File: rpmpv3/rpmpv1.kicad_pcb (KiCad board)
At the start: 2 copper layers, 85.7 x 64.4 mm, 16 parts, among them J1 RPi_GPIO, J2 RPi_GPIO, J3 TEST_1P, J4 TEST_1P, J5 TEST_1P, P1 CONN_02X25, U1 74LS245, U2 74LS245, U3 74LS245, U4 74LS245, U5 74LS05

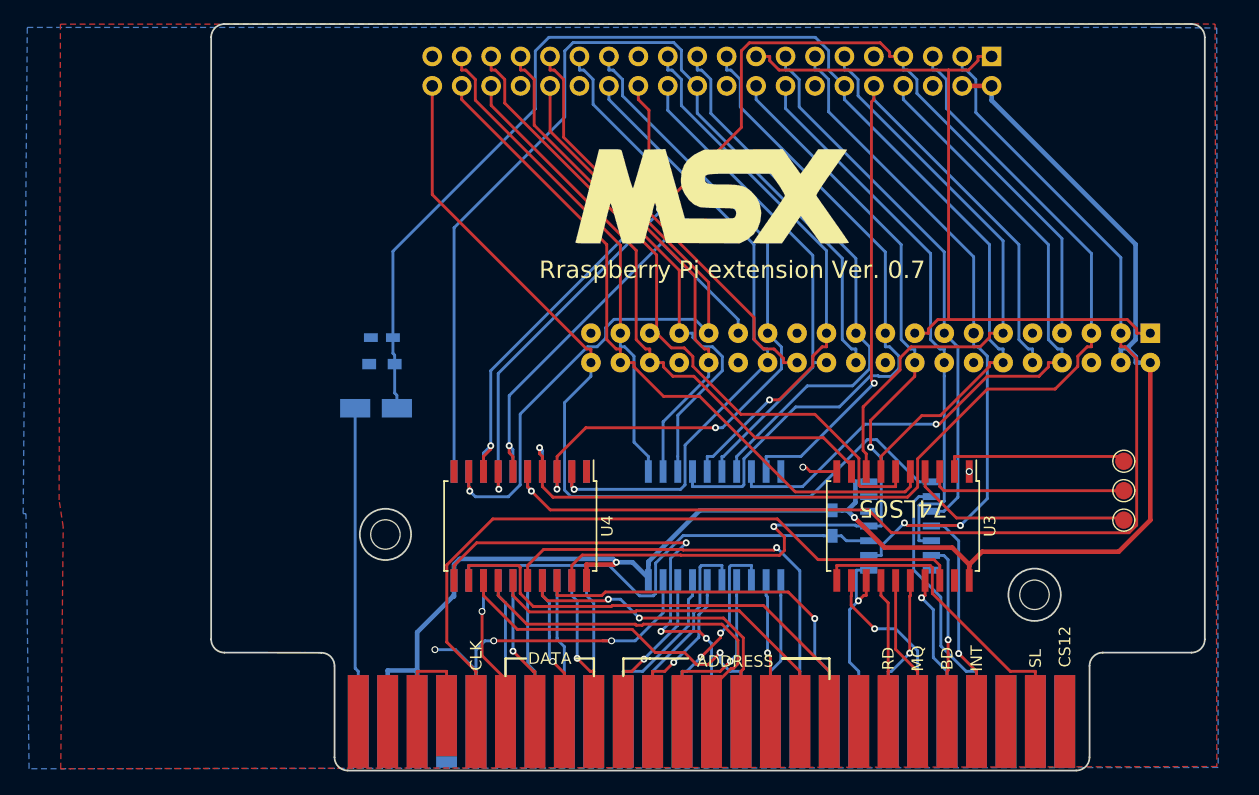
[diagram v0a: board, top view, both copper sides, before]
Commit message: update for RPMP V3
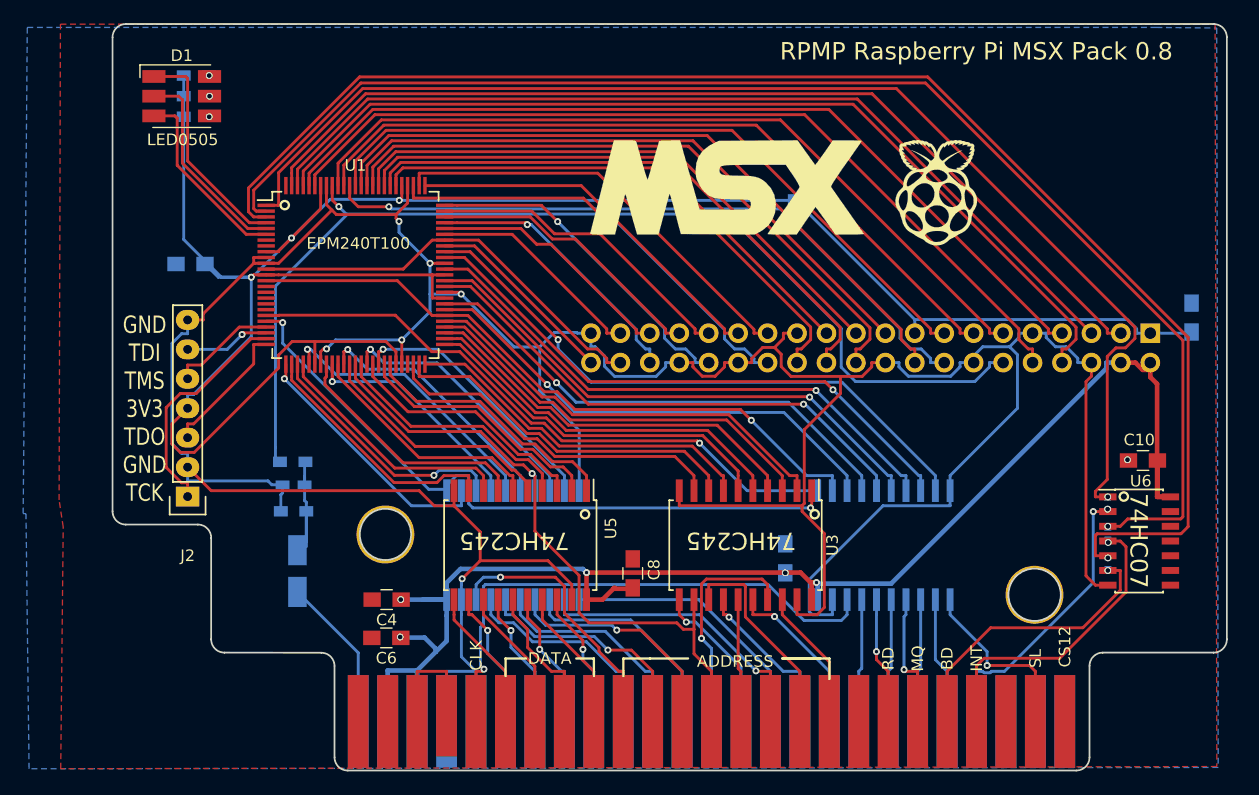
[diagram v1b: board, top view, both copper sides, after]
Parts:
- removed J3, J4, J5: TEST_1P, TestPoint:TestPoint_Pad_D1.5mm
- added C10: C, Capacitors_SMD:C_0805_HandSoldering, F.Cu at (194.7, 87.3)
- added C3: C, Capacitors_SMD:C_0805_HandSoldering, B.Cu at (112.5, 70.4)
- added C4: C, Capacitors_SMD:C_0805_HandSoldering, F.Cu at (129.4, 99.3)
- added C5: C, Capacitors_SMD:C_0805_HandSoldering, B.Cu at (166.1, 65.0)
- added C6: C, Capacitors_SMD:C_0805_HandSoldering, F.Cu at (129.4, 102.6)
- added C7: C, Capacitors_SMD:C_0805_HandSoldering, B.Cu at (198.9, 75.0)
- added C8: C, Capacitors_SMD:C_0805_HandSoldering, F.Cu at (150.7, 97.1)
- added C9: C, Capacitors_SMD:C_0805_HandSoldering, B.Cu at (163.8, 95.8)
- added D1: LED_RGB, LEDs:LED_RGB_5050-6, F.Cu at (111.8, 55.9)
- added G***: LOGO, MSX:raspberry_pi_logo, F.Cu at (176.9, 64.2)
- added G2: LOGO, MSX:msx-logo, B.Cu at (185.3, 57.2)
- added R3: R, Resistors_SMD:R_0603_HandSoldering, B.Cu at (113.0, 57.7)
- added R4: R, Resistors_SMD:R_0603_HandSoldering, B.Cu at (121.4, 91.7)
- added R5: R, Resistors_SMD:R_0402_NoSilk, B.Cu at (191.7, 96.2)
- added R6: R, Resistors_SMD:R_0402_NoSilk, B.Cu at (191.6, 91.1)
- added R7: R, Resistors_SMD:R_0402_NoSilk, B.Cu at (191.7, 93.6)
- added R8: R, Resistors_SMD:R_0603_HandSoldering, B.Cu at (121.3, 87.4)
- added U6: 74LS05, Housings_SOIC:SOIC-14_3.9x8.7mm_Pitch1.27mm, F.Cu at (194.4, 94.3)
- J2: value RPi_GPIO -> Conn_01x07; footprint Socket_Strips:Socket_Strip_Straight_2x20_Pitch2.54mm -> Pin_Headers:Pin_Header_Straight_1x07; moved to F.Cu
- U1: value 74LS245 -> MaxII_EPM240; footprint Housings_SOIC:SOIC-20W_7.5x12.8mm_Pitch1.27mm -> Housings_QFP:TQFP-100_14x14mm_Pitch0.5mm; moved to F.Cu
- U4: moved to B.Cu
- U5: value 74LS05 -> 74LS245; footprint Housings_SOIC:SOIC-14_3.9x8.7mm_Pitch1.27mm -> Housings_SOIC:SOIC-20W_7.5x12.8mm_Pitch1.27mm; moved to F.Cu
- moved J2 79.1 mm to (112.3, 90.4), turned to 180 degrees
- moved R1 67.1 mm to (113.0, 54.1), turned to 0 degrees
- moved U1 37.8 mm to (126.7, 71.3), turned to 0 degrees
- moved U5 32.8 mm to (141.0, 94.6), turned to 270 degrees
- moved U2 31.4 mm to (172.3, 94.6)
- moved R2 28.1 mm to (113.0, 55.9), turned to 0 degrees
- moved C2 15.6 mm to (121.7, 96.9), turned to 270 degrees
- moved C1 14.8 mm to (121.4, 89.4)
- moved U3 13.7 mm to (160.4, 94.6)
- moved U4 1.77 mm to (140.3, 94.6)
- moved G*** 1.48 mm to (158.8, 63.8)
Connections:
- C1 pad 1: /RC18 -> Net-(C1-Pad1)
- C2 pad 1: /RC18 -> Net-(C1-Pad1)
- J2 pad 1: +3V3 -> /TCK
- J2 pad 2: +5V -> GND
- J2 pad 3: /RD2 -> /TDO
- J2 pad 4: +5V -> +3V3
- J2 pad 5: /RD3 -> /TMS
- J2 pad 6: GND -> /TDI
- J2 pad 7: /RD4 -> GND
- R1 pad 1: /nRC24 -> +3V3
- R1 pad 2: +5V -> Net-(D1-Pad6)
- R2 pad 1: /RC18 -> +3V3
- R2 pad 2: GND -> Net-(D1-Pad5)
- U1 pad 1: /RC26 -> /WAIT3
- U1 pad 11: /A7 -> GND
- U1 pad 12: /A6 -> /RC20
- U1 pad 13: /A1 -> +3V3
- U1 pad 14: /A0 -> /CLK3
- U1 pad 15: /A3 -> Net-(U1-Pad15)
- U1 pad 16: /A2 -> Net-(U1-Pad16)
- U1 pad 17: /A5 -> Net-(U1-Pad17)
- U1 pad 18: /A4 -> Net-(U1-Pad18)
- U1 pad 19: GND -> Net-(U1-Pad19)
- U1 pad 2: /RA12 -> /INT3
- U1 pad 20: +5V -> /CD
- U1 pad 3: /RA13 -> /BUSDIR3
- U1 pad 4: /RA10 -> /LED1
- U1 pad 5: /RA11 -> /LED2
- U1 pad 6: /RA8 -> /LED3
- U1 pad 7: /RA9 -> Net-(U1-Pad7)
- U1 pad 8: /RA14 -> Net-(U1-Pad8)
- U1 pad 9: /RA15 -> +3V3
- U2 pad 1: /RC25 -> /CD
- U2 pad 11: /D1 -> /SLTSL
- U2 pad 12: /D0 -> /M1
- U2 pad 13: /D3 -> /IORQ
- U2 pad 14: /D2 -> /MREQ
- U2 pad 15: /D5 -> /WR
- U2 pad 16: /D4 -> /RD
- U2 pad 17: /D7 -> /RESET
- U2 pad 18: /D6 -> /CLK
- U2 pad 19: /nRC24 -> GND
- U2 pad 2: /RD6 -> /CLK3
- U2 pad 3: /RD7 -> /RESET3
- U2 pad 4: /RD4 -> /RD_3
- U2 pad 5: /RD5 -> /WR3
- U2 pad 6: /RD2 -> /MREQ3
- U2 pad 7: /RD3 -> /IORQ3
- U2 pad 8: /RD0 -> /M13
- U2 pad 9: /RD1 -> /SLTSL3
- U3 pad 1: GND -> /AD
- U3 pad 11: /SLTSL -> /A12
- U3 pad 12: /IORQ -> /A13
- U3 pad 13: /RESET -> /A10
- U3 pad 14: /RD -> /A11
- U3 pad 15: /MREQ -> /A8
- U3 pad 16: /WR -> /A9
- U3 pad 17: /M1 -> /A14
- U3 pad 18: /CLK -> /A15
- U3 pad 2: /TP2 -> /A153
- U3 pad 3: /TP1 -> /A143
- U3 pad 4: /TP0 -> /A93
- U3 pad 5: /RC20 -> /A83
- U3 pad 6: /RC19 -> /A113
- U3 pad 7: /RC18 -> /A103
- U3 pad 8: /RC17 -> /A133
- U3 pad 9: /RC16 -> /A123
- U4 pad 1: GND -> /AD
- U4 pad 11: /A14 -> /A7
- U4 pad 12: /A15 -> /A6
- U4 pad 13: /A12 -> /A1
- U4 pad 14: /A13 -> /A0
- U4 pad 15: /A10 -> /A3
- U4 pad 16: /A11 -> /A2
- U4 pad 17: /A8 -> /A5
- U4 pad 18: /A9 -> /A4
- U4 pad 19: /RC24 -> GND
- U4 pad 2: /RD1 -> /A43
- U4 pad 3: /RD0 -> /A53
- U4 pad 4: /RD3 -> /A23
- U4 pad 5: /RD2 -> /A33
- U4 pad 6: /RD5 -> /A03
- U4 pad 7: /RD4 -> /A13
- U4 pad 8: /RD7 -> /A63
- U4 pad 9: /RD6 -> /A73
- U5 pad 1: /RC21 -> /DD
- U5 pad 10: /nRC24 -> GND
- U5 pad 11: /RC24 -> /D6
- U5 pad 12: (no net) -> /D7
- U5 pad 13: (no net) -> /D4
- U5 pad 14: +5V -> /D5
- U5 pad 2: /WAIT -> /D13
- U5 pad 3: /RC22 -> /D03
- U5 pad 4: /INT -> /D33
- U5 pad 5: /RC23 -> /D23
- U5 pad 6: /BUSDIR -> /D53
- U5 pad 7: GND -> /D43
- U5 pad 8: /RESET -> /D73
- U5 pad 9: /RC27 -> /D63
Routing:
- net GND: track 39.2 -> 330.1 mm, vias 5 -> 7
- net /BUSDIR3: track 0.00 -> 125.8 mm, vias 0 -> 1
- net +3V3: track 65.0 -> 190.6 mm, vias 0 -> 3
- net /INT3: track 0.00 -> 118.2 mm, vias 0 -> 1
- net /WAIT3: track 0.00 -> 107.1 mm, vias 0 -> 1
- net /RC21: track 77.1 -> 16.8 mm
- net /AD: track 0.00 -> 58.9 mm, vias 0 -> 2
- net /CLK3: track 0.00 -> 57.1 mm, vias 0 -> 1
- net /CD: track 0.00 -> 53.9 mm, vias 0 -> 1
- net /SLTSL3: track 0.00 -> 52.1 mm, vias 0 -> 1
- net /M13: track 0.00 -> 50.2 mm, vias 0 -> 1
- net /IORQ3: track 0.00 -> 48.5 mm, vias 0 -> 1
- net /MREQ3: track 0.00 -> 46.8 mm, vias 0 -> 1
- net /WR3: track 0.00 -> 45.3 mm, vias 0 -> 1
- net /RD_3: track 0.00 -> 43.4 mm, vias 0 -> 1
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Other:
- board size 85.7 x 64.4 mm -> 96.1 x 64.4 mm
- board text added: "10u"
- board text added: "150R"
- board text added: "2018.03.20"
- board text added: "270R"
- board text added: "33n"
- board text added: "74HC07"
- board text added: "74HC245"
- board text added: "EPM240T100"
- board text added: "GND TDI TMS 3V3 TDO GND TCK"
- board text added: "LED0505"
- board text added: "RPMP Raspberry Pi MSX Pack 0.8"
- board text added: "Raspberry Pi MSX Pack ver. 0.8"
- board text added: "SNDIN"
- board text removed: "2018.01.19"
- board text removed: "74LS05"
- board text removed: "Rraspberry Pi extension Ver. 0.7"

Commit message: update for RPIZ80, RPIAPPLE, RPMSXP
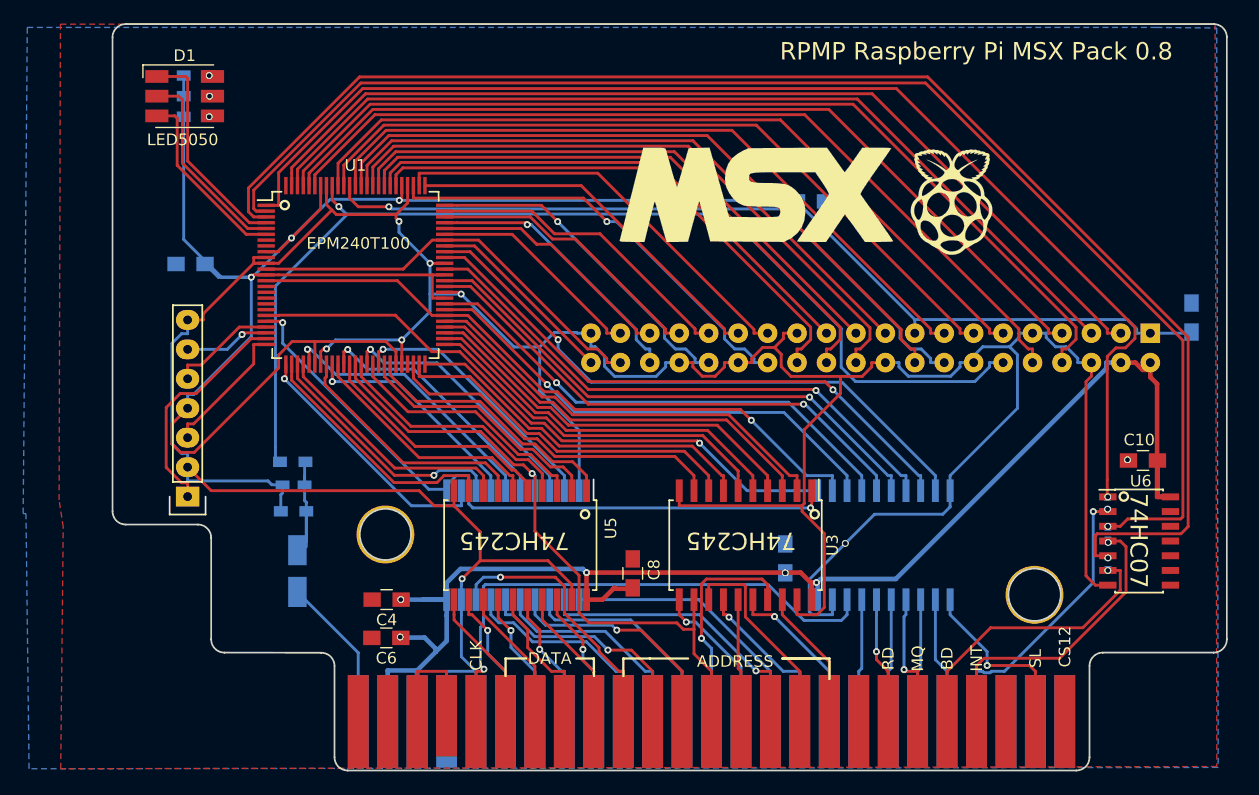
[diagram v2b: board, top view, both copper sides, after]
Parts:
- moved G*** 2.62 mm to (161.3, 64.4)
- moved G*** 1.55 mm to (178.2, 65.0)
- moved D1 0.25 mm to (112.0, 55.9)
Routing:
- net /WAIT3: track 107.1 -> 105.6 mm
- net GND: track 330.1 -> 330.2 mm, vias 7 -> 8
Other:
- board text added: "LED5050"
- board text removed: "LED0505"

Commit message: PCB files for order
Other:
- outline, holes or cut-outs redrawn
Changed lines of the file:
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@@
     (links 194)
     (no_connects 0)
-    (area 105.715999 49.581999 202.005001 114.133701)
+    (area 98.0821 49.444611 204.086546 115.286853)
     (thickness 1.6)
-    (drawings 84)
+    (drawings 79)
     (tracks 1127)
     (zones 0)
@@
     (mod_text_size 1 1)
     (mod_text_width 0.15)
-    (pad_size 2.032 1.7272)
-    (pad_drill 0.76)
+    (pad_size 5 5)
+    (pad_drill 4.5)
     (pad_to_mask_clearance 0.2)
     (aux_axis_origin 0 0)
@@
     (pcbplotparams
       (layerselection 0x010f0_80000001)
-      (usegerberextensions false)
+      (usegerberextensions true)
       (excludeedgelayer true)
       (linewidth 0.100000)
@@
     (fp_circle (center -26.873455 -12.985388) (end -25.523455 -12.985388) (layer Dwgs.User) (width 0.1))
     (fp_arc (start 32.846865 7.356852) (end 32.846865 8.356852) (angle -90) (layer Dwgs.User) (width 0.1))
-    (pad "" np_thru_hole circle (at 29.12364 -7.78256) (size 5 5) (drill 4.5) (layers *.Cu *.Mask F.SilkS))
+    (pad "" thru_hole circle (at 29.12364 -7.78256) (size 5 5) (drill 4.5) (layers *.Cu *.Mask))
     (pad 1 connect rect (at 31.73984 3.14744) (size 1.8 8) (layers B.Cu B.Mask)
       (net 55 "Net-(P1-Pad1)"))
@@
     (pad 50 connect rect (at -29.22016 3.14744) (size 1.8 8) (layers F.Cu F.Mask)
       (net 62 "Net-(P1-Pad50)"))
-    (pad "" np_thru_hole circle (at -26.87574 -12.98448) (size 5 5) (drill 4.5) (layers *.Cu *.Mask F.SilkS))
+    (pad "" thru_hole circle (at -26.87574 -12.98448) (size 5 5) (drill 4.5) (layers *.Cu *.Mask))
   )
   (module Capacitors_SMD:C_0603_HandSoldering (layer B.Cu)
@@
     )
   )
-  (dimension 11.557 (width 0.3) (layer Dwgs.User)
-    (gr_text "11.557 mm" (at 112.2045 44.116) (layer Dwgs.User)
-      (effects (font (size 1.5 1.5) (thickness 0.3)))
-    )
-    (feature1 (pts (xy 117.983 51.054) (xy 117.983 42.766)))
-    (feature2 (pts (xy 106.426 51.054) (xy 106.426 42.766)))
-    (crossbar (pts (xy 106.426 45.466) (xy 117.983 45.466)))
-    (arrow1a (pts (xy 117.983 45.466) (xy 116.856496 46.052421)))
-    (arrow1b (pts (xy 117.983 45.466) (xy 116.856496 44.879579)))
-    (arrow2a (pts (xy 106.426 45.466) (xy 107.552504 46.052421)))
-    (arrow2b (pts (xy 106.426 45.466) (xy 107.552504 44.879579)))
-  )
   (gr_text 10u (at 117.3226 96.4692) (layer B.SilkS)
     (effects (font (size 1 1) (thickness 0.25)) (justify mirror))
@@
     (effects (font (size 1.5 1.2) (thickness 0.3)) (justify mirror))
   )
-  (gr_text EPM240T100 (at 127 68.58) (layer F.SilkS)
+  (gr_text EPM240T100 (at 127.127 71.501) (layer F.SilkS)
     (effects (font (size 1 1) (thickness 0.25)))
   )
@@
     (effects (font (size 1 1) (thickness 0.25)) (justify mirror))
   )
-  (dimension 100.838 (width 0.3) (layer Dwgs.User)
-    (gr_text "100.838 mm" (at 151.511 40.052) (layer Dwgs.User)
-      (effects (font (size 1.5 1.5) (thickness 0.3)))
-    )
-    (feature1 (pts (xy 201.93 48.514) (xy 201.93 38.702)))
-    (feature2 (pts (xy 101.092 48.514) (xy 101.092 38.702)))
-    (crossbar (pts (xy 101.092 41.402) (xy 201.93 41.402)))
-    (arrow1a (pts (xy 201.93 41.402) (xy 200.803496 41.988421)))
-    (arrow1b (pts (xy 201.93 41.402) (xy 200.803496 40.815579)))
-    (arrow2a (pts (xy 101.092 41.402) (xy 102.218504 41.988421)))
-    (arrow2b (pts (xy 101.092 41.402) (xy 102.218504 40.815579)))
-  )
   (gr_text "Raspberry Pi \nMSX Pack ver. 0.8" (at 170.18 59.436) (layer B.SilkS)
     (effects (font (size 1.5 1.5) (thickness 0.3)) (justify left mirror))
@@
     (effects (font (size 1.5 1.5) (thickness 0.3)) (justify mirror))
   )
-  (gr_circle (center 129.3368 93.6879) (end 130.9878 95.1611) (layer Edge.Cuts) (width 0.15))
   (gr_line (start 106.934 92.837) (end 113.157 92.837) (layer Edge.Cuts) (width 0.15))
   (gr_line (start 114.3 102.743) (end 114.3 93.98) (layer Edge.Cuts) (width 0.15))
@@
     (effects (font (size 1.5 1.5) (thickness 0.3)))
   )
-  (dimension 83.388363 (width 0.3) (layer Cmts.User)
-    (gr_text "83.388 mm" (at 222.208296 72.085548 270.1134396) (layer Cmts.User)
-      (effects (font (size 1.5 1.5) (thickness 0.3)))
-    )
-    (feature1 (pts (xy 215.8873 30.4038) (xy 223.475744 30.388775)))
-    (feature2 (pts (xy 216.0524 113.792) (xy 223.640844 113.776975)))
-    (crossbar (pts (xy 220.940849 113.782321) (xy 220.775749 30.394121)))
-    (arrow1a (pts (xy 220.775749 30.394121) (xy 221.364399 31.519462)))
-    (arrow1b (pts (xy 220.775749 30.394121) (xy 220.19156 31.521784)))
-    (arrow2a (pts (xy 220.940849 113.782321) (xy 221.525038 112.654658)))
-    (arrow2b (pts (xy 220.940849 113.782321) (xy 220.352199 112.65698)))
-  )
-  (gr_circle (center 185.3438 98.8949) (end 187.1472 100.2538) (layer Edge.Cuts) (width 0.15))
   (gr_arc (start 200.787 50.8) (end 200.787 49.657) (angle 90) (layer Edge.Cuts) (width 0.15))
   (gr_arc (start 106.934 50.8) (end 105.791 50.8) (angle 90) (layer Edge.Cuts) (width 0.15))
